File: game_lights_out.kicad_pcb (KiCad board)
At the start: 2 copper layers, 171.2 x 136.9 mm, 98 parts, among them SW1 SW_MEC_5E, SW10 SW_MEC_5E, SW11 SW_MEC_5E, SW12 SW_MEC_5E, SW13 SW_MEC_5E, SW14 SW_MEC_5E, SW15 SW_MEC_5E, SW16 SW_MEC_5E, SW17 SW_MEC_5E, SW18 SW_MEC_5E, SW19 SW_MEC_5E, SW2 SW_MEC_5E, SW20 SW_MEC_5E, SW21 SW_MEC_5E, SW22 SW_MEC_5E, SW23 SW_MEC_5E, SW24 SW_MEC_5E, SW25 SW_MEC_5E, SW26 SW_MEC_5E, SW27 SW_MEC_5E, SW28 SW_MEC_5E, SW29 SW_MEC_5E, SW3 SW_MEC_5E, SW30 SW_MEC_5E, SW31 SW_MEC_5E, SW32 SW_MEC_5E, SW33 SW_MEC_5E, SW34 SW_MEC_5E, SW35 SW_MEC_5E, SW36 SW_MEC_5E, SW37 SW_MEC_5E, SW38 SW_MEC_5E, SW39 SW_MEC_5E, SW4 SW_MEC_5E, SW40 SW_MEC_5E, SW5 SW_MEC_5E, SW6 SW_MEC_5E, SW7 SW_MEC_5E, SW8 SW_MEC_5E, SW9 SW_MEC_5E, U1 ATmega328-P, U2 ULN2803A

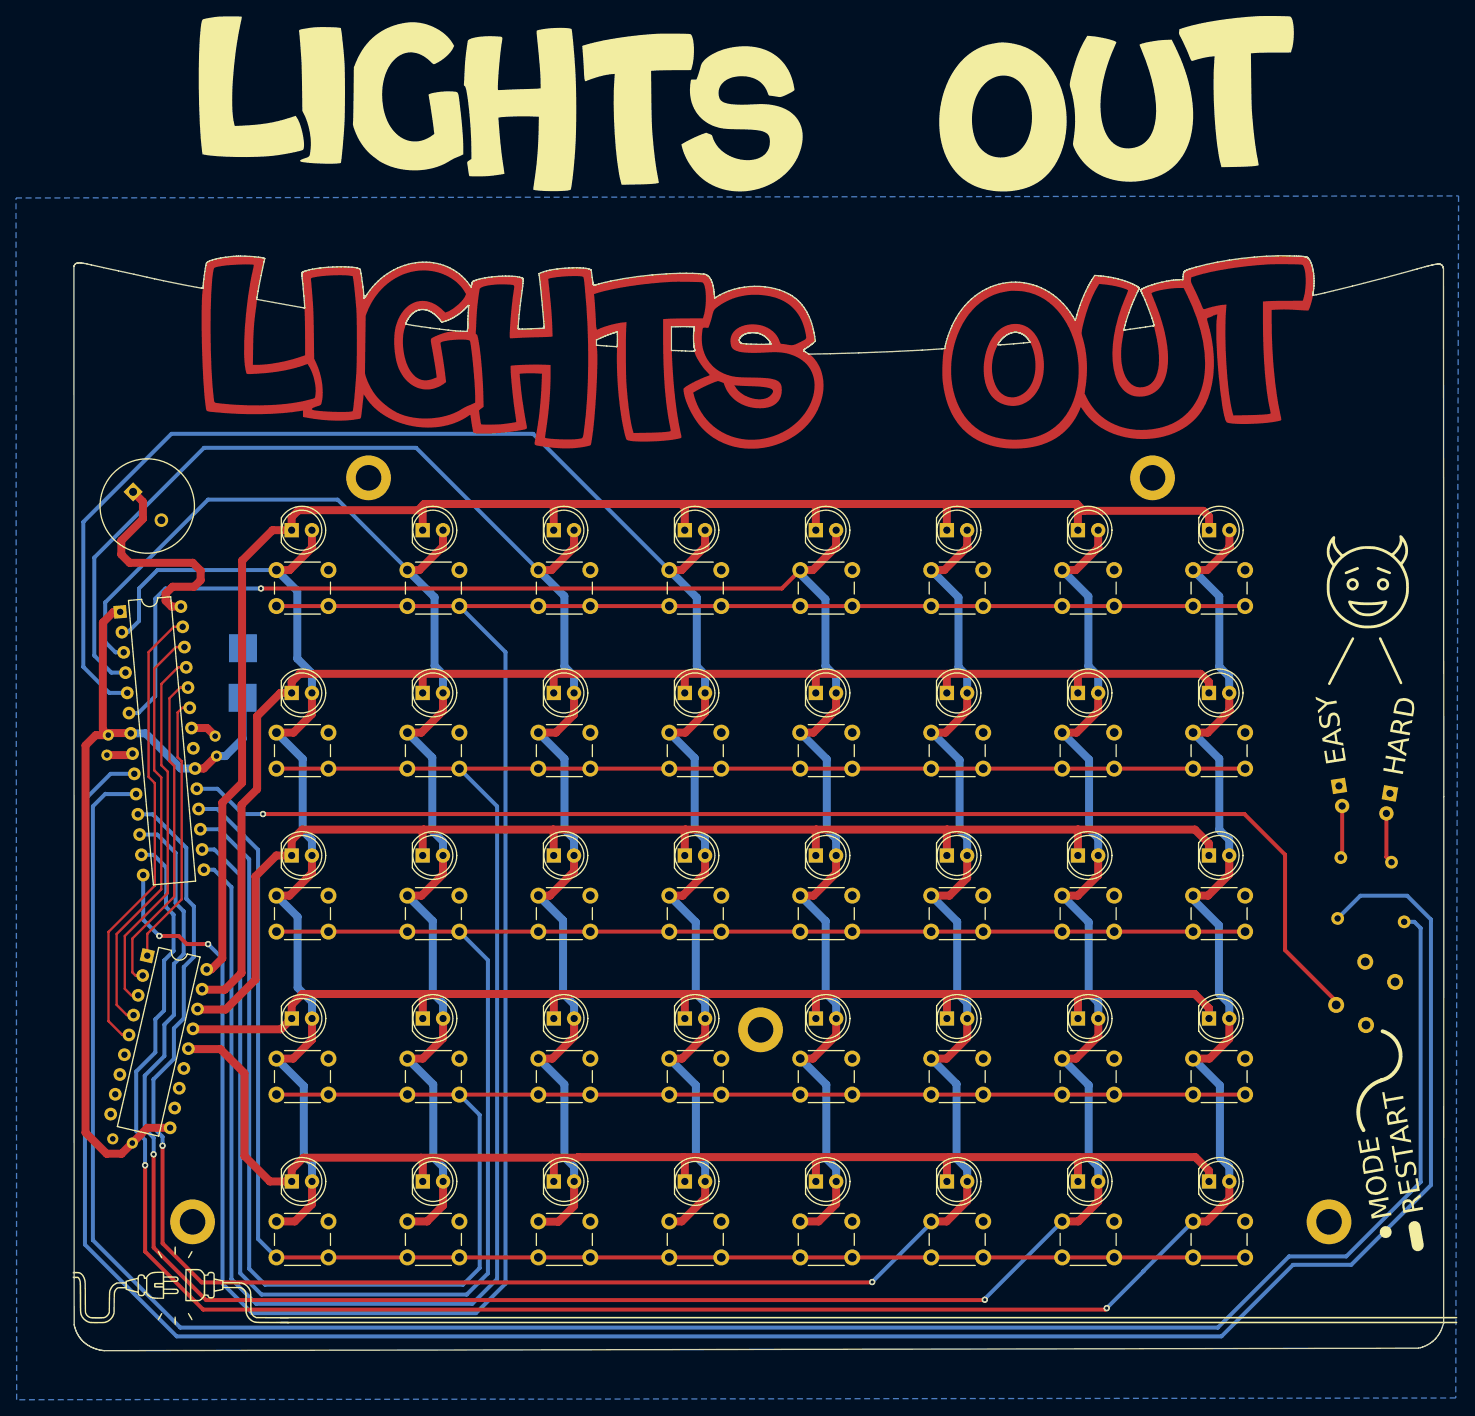
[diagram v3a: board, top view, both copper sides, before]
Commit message: Added order number placeholder (+ small fixes)
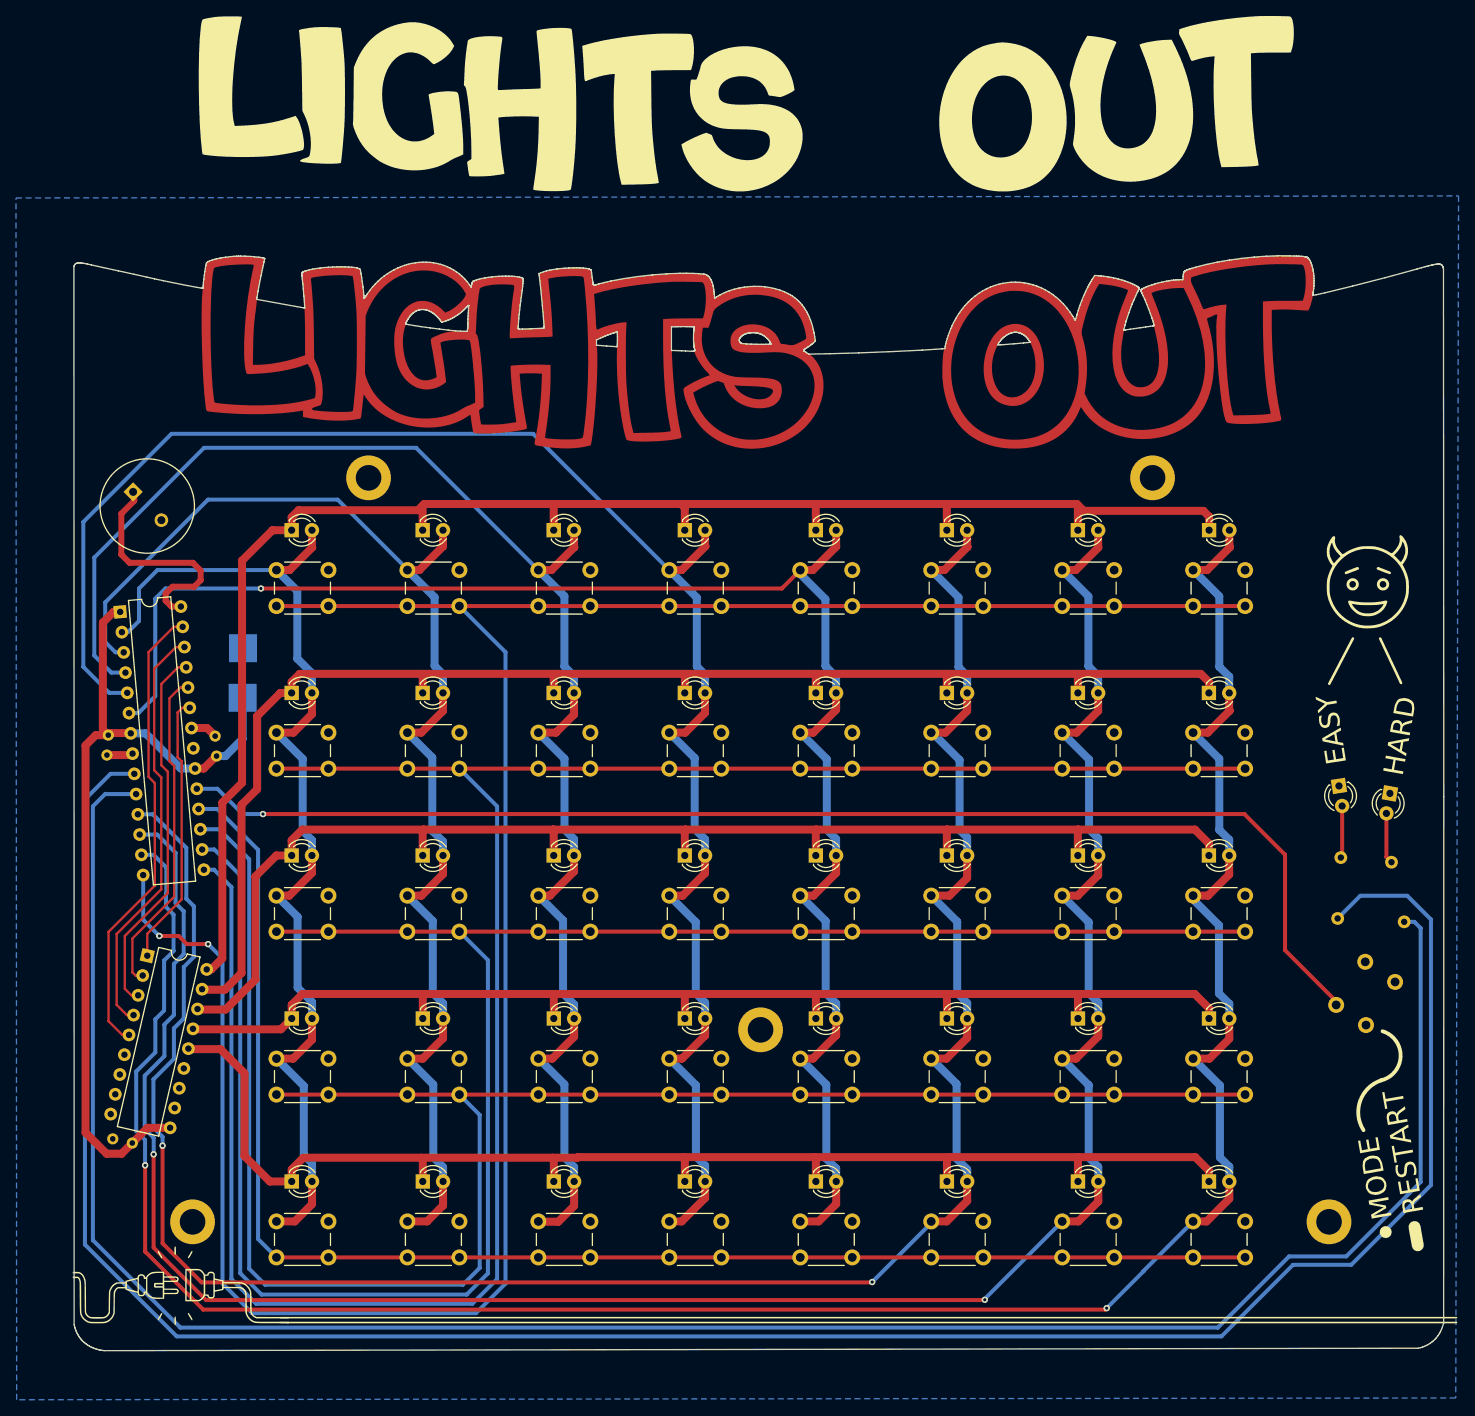
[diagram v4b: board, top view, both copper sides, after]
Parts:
- D1, D10, D11, D12, D13, D14, D15, D16, D17, D18, D19, D2, D20, D21, D22, D23, D24, D25, D26, D27, D28, D29, D3, D30, D31, D32, D33, D34, D35, D36, D37, D38, D39, D4, D40, D5, D6, D7, D8, D9: footprint LED_THT:LED_D5.0mm -> LED_THT:LED_D3.0mm
- DMOD1, DMOD2: footprint LED_THT:LED_D1.8mm_W3.3mm_H2.4mm -> LED_THT:LED_D3.0mm
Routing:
- net SPK: track 29.3 -> 28.7 mm
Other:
- board text added: "JLCJLCJLCJLC"

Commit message: Minor tweaks
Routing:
- net LD1: track 291.3 -> 268.7 mm
- net LD2: track 272.4 -> 274.8 mm
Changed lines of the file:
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@@
   (segment (start 152.77 139.91) (end 136.64 139.91) (width 1) (layer "F.Cu") (net 14))
   (segment (start 90.12 139.99) (end 87.01 139.99) (width 1) (layer "F.Cu") (net 14))
+  (segment (start 34.721376 92.000334) (end 31.749666 92.000334) (width 0.5) (layer "B.Cu") (net 15))
+  (segment (start 170.615 162.32) (end 179.56 153.375) (width 0.5) (layer "B.Cu") (net 15))
   (segment (start 28.55 95.2) (end 28.55 150.85) (width 0.5) (layer "B.Cu") (net 15))
-  (segment (start 187.975379 107.24) (end 185.1356 110.079779) (width 0.5) (layer "B.Cu") (net 15))
+  (segment (start 179.56 153.375) (end 179.56 114.8) (width 0.5) (layer "B.Cu") (net 15))
+  (segment (start 184.280221 110.079779) (end 185.1356 110.079779) (width 0.5) (layer "B.Cu") (net 15))
+  (segment (start 40.02 162.32) (end 170.615 162.32) (width 0.5) (layer "B.Cu") (net 15))
   (segment (start 28.55 150.85) (end 40.02 162.32) (width 0.5) (layer "B.Cu") (net 15))
-  (segment (start 196.8 143.41) (end 196.8 110.21) (width 0.5) (layer "B.Cu") (net 15))
+  (segment (start 179.56 114.8) (end 184.280221 110.079779) (width 0.5) (layer "B.Cu") (net 15))
   (segment (start 31.749666 92.000334) (end 28.55 95.2) (width 0.5) (layer "B.Cu") (net 15))
-  (segment (start 34.721376 92.000334) (end 31.749666 92.000334) (width 0.5) (layer "B.Cu") (net 15))
-  (segment (start 40.02 162.32) (end 170.615 162.32) (width 0.5) (layer "B.Cu") (net 15))
-  (segment (start 193.83 107.24) (end 187.975379 107.24) (width 0.5) (layer "B.Cu") (net 15))
-  (segment (start 196.8 110.21) (end 193.83 107.24) (width 0.5) (layer "B.Cu") (net 15))
-  (segment (start 170.615 162.32) (end 179.56 153.375) (width 0.5) (layer "B.Cu") (net 15))
-  (segment (start 186.835 153.375) (end 196.8 143.41) (width 0.5) (layer "B.Cu") (net 15))
-  (segment (start 179.56 153.375) (end 186.835 153.375) (width 0.5) (layer "B.Cu") (net 15))
   (segment (start 32.950371 71.757658) (end 32.128342 71.757658) (width 1) (layer "F.Cu") (net 16))
   (segment (start 31.727618 86.902623) (end 34.278625 86.902623) (width 1) (layer "F.Cu") (net 16))
@@
   (segment (start 48.26 87.63) (end 48.26 81.8896) (width 1) (layer "B.Cu") (net 16))
   (segment (start 48.3108 83.1596) (end 47.6504 82.4992) (width 1) (layer "B.Cu") (net 16))
-  (segment (start 194.721743 110.501743) (end 193.452144 110.501743) (width 0.5) (layer "B.Cu") (net 17))
-  (segment (start 195.51 111.29) (end 194.721743 110.501743) (width 0.5) (layer "B.Cu") (net 17))
-  (segment (start 195.51 143.025) (end 195.51 111.29) (width 0.5) (layer "B.Cu") (net 17))
+  (segment (start 29.54 96.06) (end 29.54 150.29) (width 0.5) (layer "B.Cu") (net 17))
+  (segment (start 193.452144 109.392144) (end 193.452144 110.501743) (width 0.5) (layer "B.Cu") (net 17))
+  (segment (start 178.385 114.2) (end 184.235 108.35) (width 0.5) (layer "B.Cu") (net 17))
+  (segment (start 184.235 108.35) (end 192.41 108.35) (width 0.5) (layer "B.Cu") (net 17))
+  (segment (start 192.41 108.35) (end 193.452144 109.392144) (width 0.5) (layer "B.Cu") (net 17))
   (segment (start 31.1 94.5) (end 29.54 96.06) (width 0.5) (layer "B.Cu") (net 17))
-  (segment (start 29.54 96.06) (end 29.54 150.29) (width 0.5) (layer "B.Cu") (net 17))
-  (segment (start 179.06 152.325) (end 186.21 152.325) (width 0.5) (layer "B.Cu") (net 17))
+  (segment (start 31.130669 94.530669) (end 31.1 94.5) (width 0.5) (layer "B.Cu") (net 17))
+  (segment (start 178.385 152.8) (end 178.385 114.2) (width 0.5) (layer "B.Cu") (net 17))
+  (segment (start 34.942751 94.530669) (end 31.130669 94.530669) (width 0.5) (layer "B.Cu") (net 17))
+  (segment (start 40.47 161.22) (end 169.965 161.22) (width 0.5) (layer "B.Cu") (net 17))
+  (segment (start 169.965 161.22) (end 178.385 152.8) (width 0.5) (layer "B.Cu") (net 17))
   (segment (start 29.54 150.29) (end 40.47 161.22) (width 0.5) (layer "B.Cu") (net 17))
-  (segment (start 40.47 161.22) (end 170.165 161.22) (width 0.5) (layer "B.Cu") (net 17))
-  (segment (start 170.165 161.22) (end 179.06 152.325) (width 0.5) (layer "B.Cu") (net 17))
-  (segment (start 34.942751 94.530669) (end 31.130669 94.530669) (width 0.5) (layer "B.Cu") (net 17))
-  (segment (start 31.130669 94.530669) (end 31.1 94.5) (width 0.5) (layer "B.Cu") (net 17))
-  (segment (start 186.21 152.325) (end 195.51 143.025) (width 0.5) (layer "B.Cu") (net 17))
   (segment (start 75.357145 71.03) (end 85.225716 71.03) (width 0.5) (layer "F.Cu") (net 18))
   (segment (start 134.331429 71.03) (end 140.831429 71.03) (width 0.5) (layer "F.Cu") (net 18))

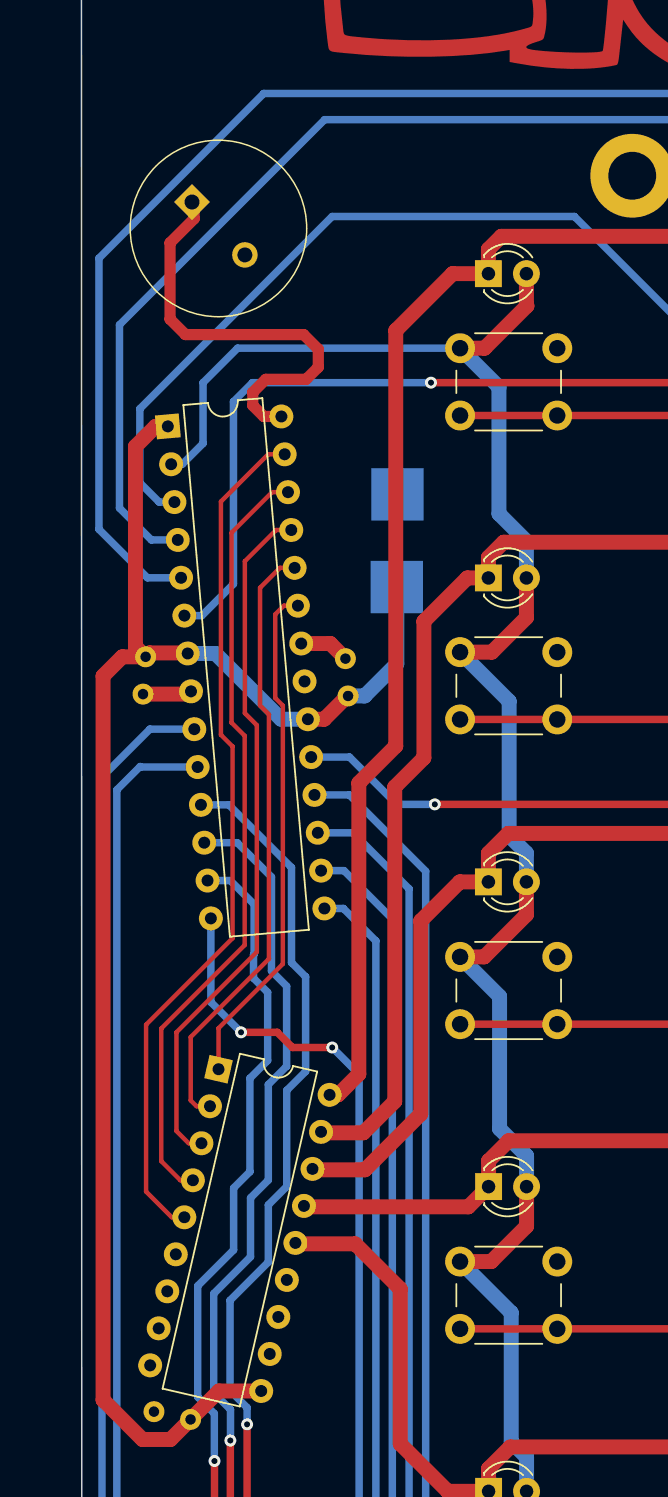
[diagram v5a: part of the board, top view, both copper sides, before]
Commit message: Added reset pull up resitor
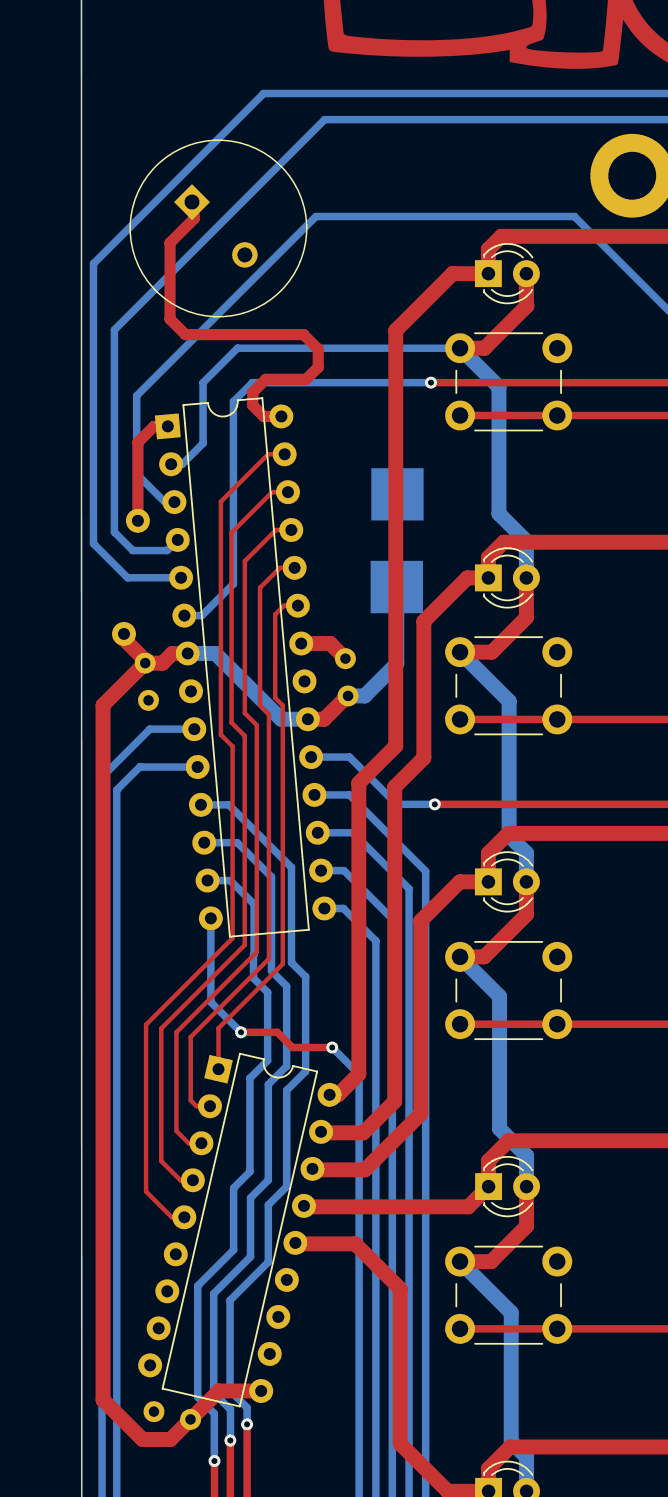
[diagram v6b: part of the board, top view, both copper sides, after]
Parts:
- added R1: 10K, Resistor_THT:R_Axial_DIN0207_L6.3mm_D2.5mm_P7.62mm_Horizontal, F.Cu at (30.0, 85.6)
- moved C3 0.42 mm to (31.4, 87.6), turned to -85 degrees
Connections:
- C1 pad 1: RST -> VCC
- C2 pad 1: RST -> VCC
- C3 pad 1: RST -> VCC
- REF** pad 1: RST -> VCC
- U1 pad 20: RST -> VCC
- U1 pad 7: RST -> VCC
- U2 pad 10: RST -> VCC
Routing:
- net RST: track 108.8 -> 7.68 mm
- net VCC: track 0.00 -> 93.1 mm
- net GND: track 6.66 -> 3.66 mm
- net C3: track 193.3 -> 195.3 mm
- net C4: track 217.8 -> 218.9 mm
- net C2: track 163.1 -> 163.7 mm
